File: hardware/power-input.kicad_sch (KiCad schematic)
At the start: 28 parts

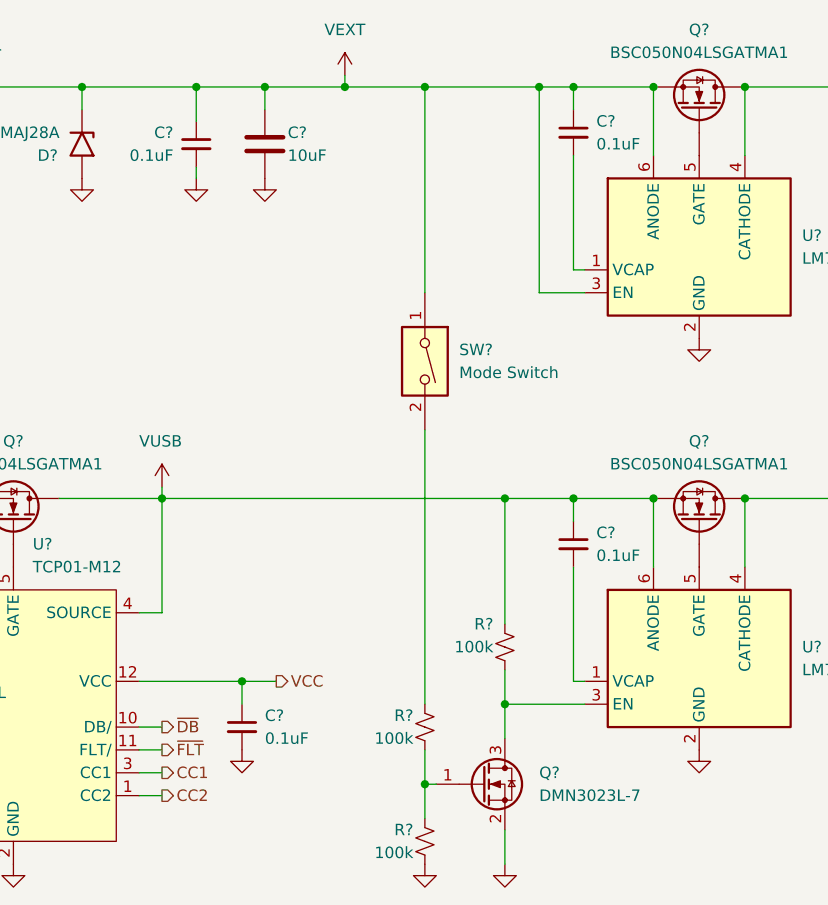
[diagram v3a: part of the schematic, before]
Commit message: Create MCU schematic
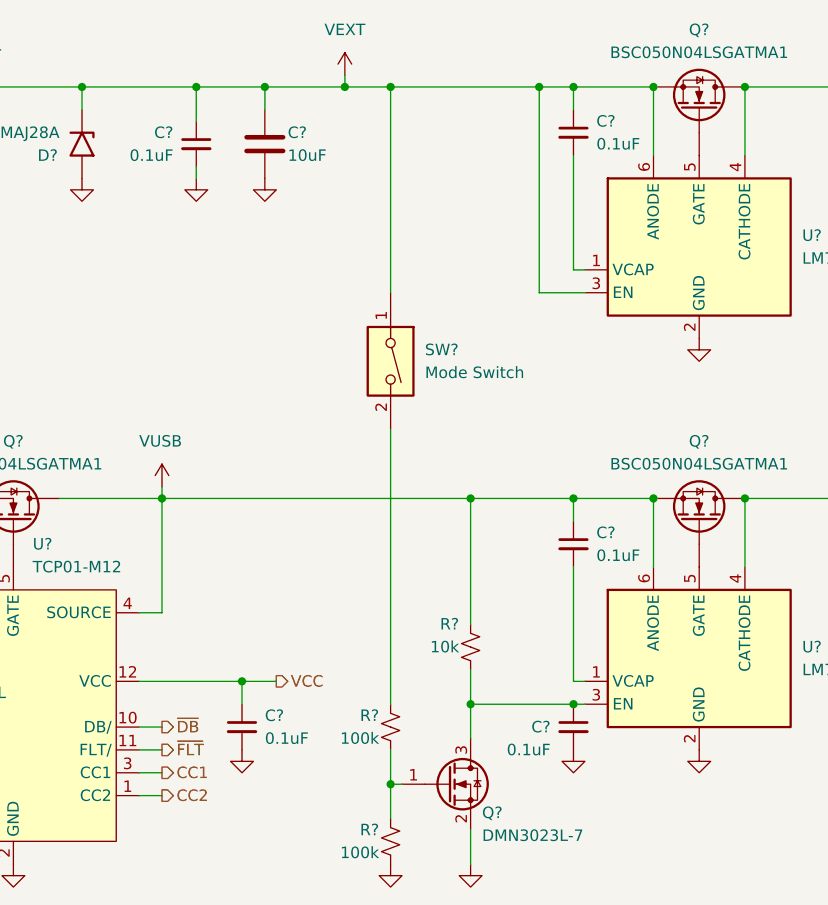
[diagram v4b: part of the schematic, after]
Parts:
- added C?: 0.1uF, Capacitor_SMD:C_0603_1608Metric_Pad1.08x0.95mm_HandSolder, symbol Device:C_Small
- R?: value 100k -> 10k
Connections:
- net GND: now also C?.2
- net at Q?.3 (D), R?.2, U?.3 (EN): now also C?.1
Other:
- title: Power Input -> Power Input & Source Select
- moved on the sheet: Q?, R?, SW?
